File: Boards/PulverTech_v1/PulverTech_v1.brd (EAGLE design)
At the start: 87.6 x 61.6 mm, 40 parts, among them IC1 786TV, K1 G5LE, P1 FSMCD, Q1 16.0 mHz, Q10 BC548, Q2 BC548, Q3 BC548, Q4 BC548, Q6 IRF540, Q7 IRF540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

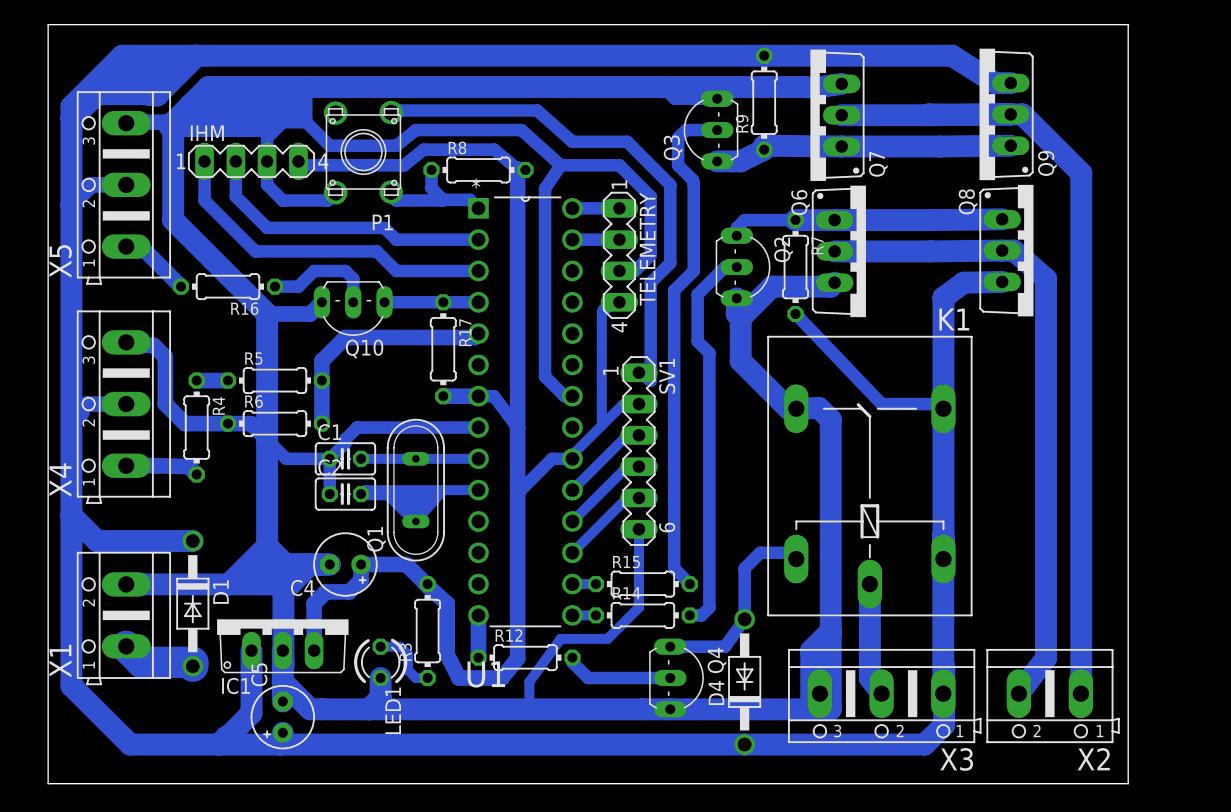
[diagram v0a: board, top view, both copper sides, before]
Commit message: Add optocouplers, changed sensor input for flux and minor changes
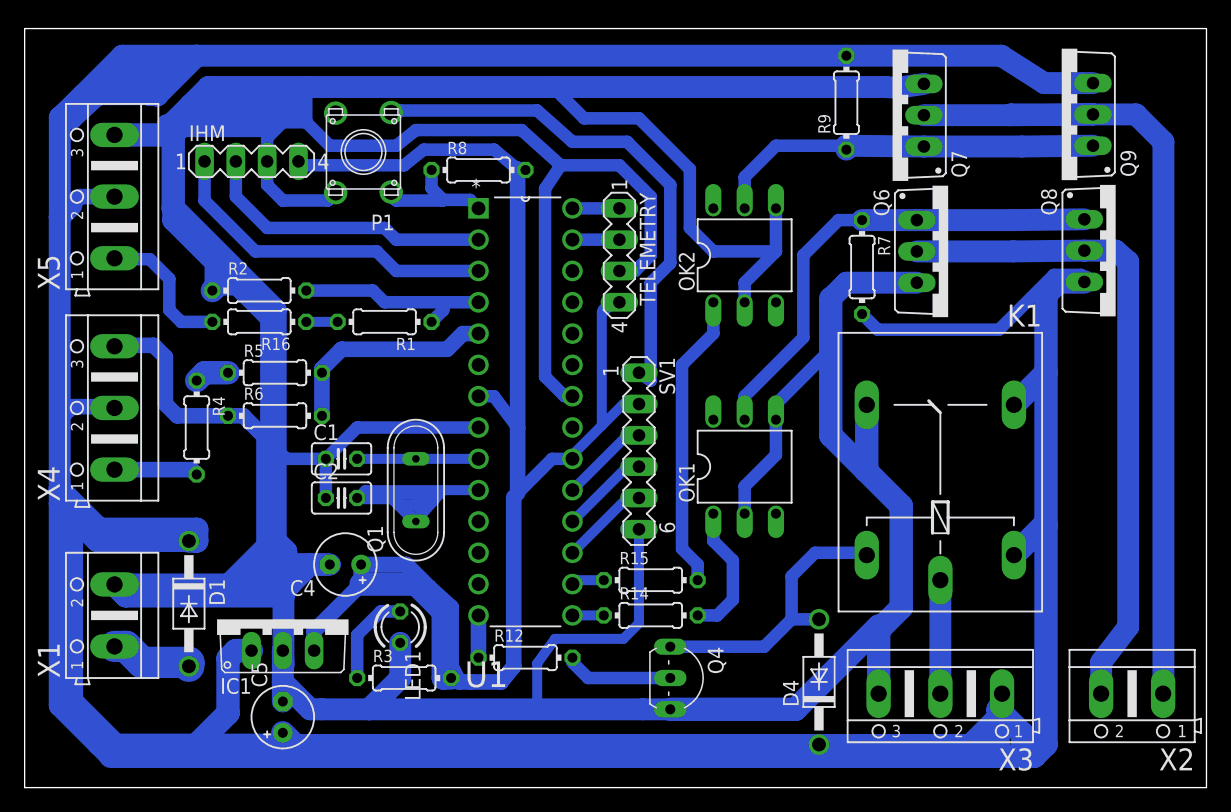
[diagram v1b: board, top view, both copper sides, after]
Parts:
- removed Q10, Q2, Q3: BC548, transistor-npn:TO92-EBC
- removed R17: 1k, eagle-ltspice:0204/7
- added OK1, OK2: 4N25M, optocoupler:DIL06
- added R1, R2: 10k, eagle-ltspice:0204/7
- D1: value 1N4004 -> 1N4007
- R16: value 1k -> 10k
- moved Q6 6.67 mm to (73.3, 43.5)
- moved Q7 6.67 mm to (68.8, 54.5)
- moved Q8 6.67 mm to (86.9, 43.6)
- moved Q9 6.67 mm to (82.5, 54.6)
- moved R9 6.67 mm to (65.1, 55.6)
- moved X2 6.67 mm to (88.3, 7.62)
- moved D4 6.03 mm to (62.9, 8.57)
- moved K1 5.72 mm to (72.7, 26.4)
- moved R7 5.40 mm to (66.4, 42.2)
- moved X3 4.76 mm to (72.7, 7.62)
- moved R3 4.26 mm to (29.2, 8.89), turned to 0 degrees
- moved R16 3.82 mm to (17.5, 37.8)
- moved LED1 3.27 mm to (28.9, 13.0)
- moved X5 1.35 mm to (5.71, 47.9)
- moved X4 1.00 mm to (5.71, 30.8)
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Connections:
- removed net N$38: Q2.C, Q6.G, Q8.G, R7.1
- removed net N$7: Q3.B, R15.2
- new net N$16: OK1.1, R14.2
- new net N$17: OK2.1, R15.2
- net GND: now also OK1.2, OK1.4, OK2.2, OK2.4, R2.1; no longer Q10.E, Q2.E, Q3.E
- net N$15: now also OK1.5, Q6.G, Q8.G, R7.1; no longer Q2.B, R14.2
- net N$39: now also OK2.5; no longer Q3.C
- net N$4: now also R1.2; no longer Q10.B
- net SENSOR_FLUX: now also R1.1, R2.2; no longer Q10.C, R17.1
- net VCC: no longer R17.2
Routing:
- net VIN: track 329.7 -> 469.3 mm
- net GND: track 445.7 -> 564.7 mm
- net N$7: track 41.3 -> 0.00 mm
- net N$17: track 0.00 -> 24.1 mm
- net N$38: track 22.4 -> 0.00 mm
- net VCC: track 120.4 -> 133.1 mm
- net N$16: track 0.00 -> 11.0 mm
- net SENSOR_FLUX: track 7.62 -> 16.3 mm
- net N$39: track 24.4 -> 32.2 mm
- net N$15: track 31.7 -> 39.3 mm
- net N$12: track 5.79 -> 13.1 mm
- net N$33: track 16.4 -> 23.5 mm
- net N$4: track 9.04 -> 2.54 mm
- net N$9: track 5.61 -> 7.77 mm
- net MOTOR_B: track 71.0 -> 72.4 mm
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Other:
- board size 87.6 x 61.6 mm -> 95.9 x 61.6 mm
